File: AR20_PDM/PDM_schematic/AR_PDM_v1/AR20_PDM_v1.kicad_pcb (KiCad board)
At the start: 2 copper layers, 118 x 112 mm, 253 parts, among them IC1 TMUX1208PWR, J1 S_T_?, J2 1-776163-1, K1 DIPxx-1Cxx-51x, K2 DIPxx-1Cxx-51x, P1 B4B-PH-SM4-TB, Q1 BTS50025-1TAD, Q2 BTS50025-1TAD, Q3 BTS50025-1TAD, Q5 BTS50025-1TAD, Q6 BTS50025-1TAD, Q7 BTS50025-1TAD, Q8 BTS50025-1TAD, SW1 SW_DIP_x07, U1 ACM_2020, U10 N-MOS, U11 N-MOS, U12 P-MOS, U13 N-MOS, U14 N-MOS, U15 NMOS, U16 NMOS, U17 NMOS, U18 NMOS, U19 NMOS, U2 INA233, U20 NMOS, U21 NMOS, U22 NMOS, U23 NMOS, U24 NMOS, U25 NMOS, U26 NMOS, U27 NMOS, U28 NMOS, U29 INA233, U3 INA233, U30 INA233, U31 INA233, U32 Fet-P, U33 Fet-P, U34 Fet-P, U35 Fet-P, U36 Fet-P, U4 INA233, U5 INA233, U6 INA233, U7 INA233, U8 INA233, U9 TCA6424ARGJR

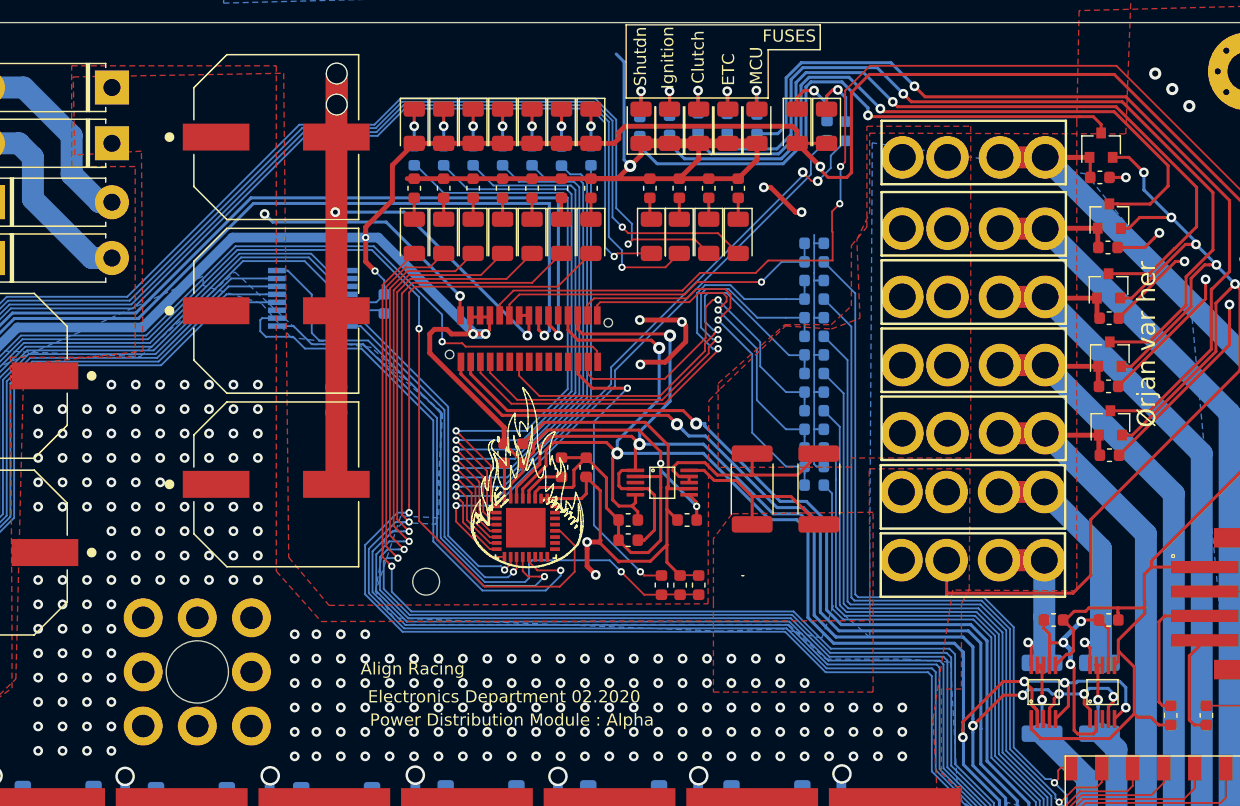
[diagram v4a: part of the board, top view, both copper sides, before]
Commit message: misc silkscreen changes
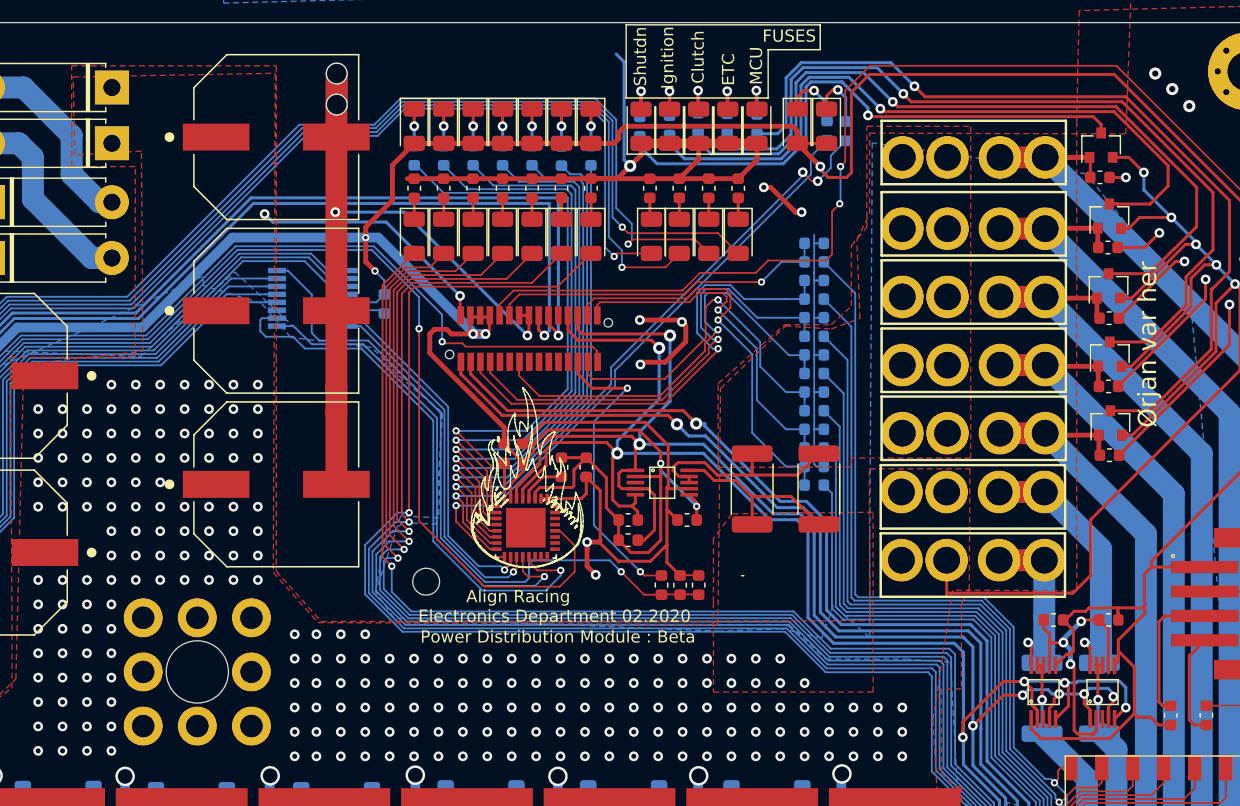
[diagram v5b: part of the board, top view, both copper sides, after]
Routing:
- net V+12V: vias 243 -> 244
- net (no net): vias 1 -> 0
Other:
- board text added: "Power Distribution Module : Beta"
- board text removed: "Power Distribution Module : Alpha"
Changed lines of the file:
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@@
     (thickness 1.6)
     (drawings 3807)
-    (tracks 3381)
+    (tracks 3380)
     (zones 0)
     (modules 253)
@@
     (34 B.Paste user hide)
     (35 F.Paste user hide)
-    (36 B.SilkS user hide)
-    (37 F.SilkS user hide)
+    (36 B.SilkS user)
+    (37 F.SilkS user)
     (38 B.Mask user hide)
     (39 F.Mask user hide)
@@
   (gr_line (start 88.955326 68.656325) (end 88.955666 69.225376) (layer F.SilkS) (width 0.06))
   (gr_arc (start 89.985704 70.027356) (end 87.409482 69.255581) (angle -5.477121106) (layer F.SilkS) (width 0.06))
-  (gr_text "Align Racing" (at 79.502 89.281) (layer F.SilkS)
+  (gr_text "Align Racing" (at 88.1507 83.3628) (layer F.SilkS)
     (effects (font (size 1 1) (thickness 0.15)))
   )
-  (gr_text "Power Distribution Module : Alpha" (at 87.63 93.472) (layer F.SilkS)
+  (gr_text "Power Distribution Module : Beta" (at 91.4019 86.6648) (layer F.SilkS)
     (effects (font (size 1 1) (thickness 0.15)))
   )
-  (gr_text "Ørjan var her" (at 139.6238 62.6999 90) (layer F.SilkS)
+  (gr_text "Ørjan var her" (at 139.7127 62.7126 90) (layer F.SilkS)
     (effects (font (size 1.5 1.5) (thickness 0.3)))
   )
-  (gr_text "Electronics Department 02.2020" (at 86.995 91.567) (layer F.SilkS)
+  (gr_text "Electronics Department 02.2020" (at 91.1225 84.963) (layer F.SilkS)
     (effects (font (size 1 1) (thickness 0.15)))
   )
@@
   (gr_line (start 151.8574 36.337) (end 33.857 36.337) (layer Edge.Cuts) (width 0.05))
   (gr_line (start 151.8574 148.336) (end 151.8574 36.337) (layer Edge.Cuts) (width 0.05))
-  (via (at 69.8373 96.4489) (size 0.8) (drill 0.4) (layers F.Cu B.Cu) (net 0))
+  (via (at 69.8373 96.4489) (size 0.8) (drill 0.4) (layers F.Cu B.Cu) (net 1))
   (via (at 69.8373 86.4489) (size 0.8) (drill 0.4) (layers F.Cu B.Cu) (net 1))
   (via (at 69.8373 88.4489) (size 0.8) (drill 0.4) (layers F.Cu B.Cu) (net 1))
@@
   (segment (start 114.554 48.133) (end 114.554 51.117502) (width 0.15) (layer B.Cu) (net 92))
   (segment (start 114.554 51.117502) (end 114.490502 51.181) (width 0.15) (layer B.Cu) (net 92))
-  (segment (start 113.8555 51.816002) (end 114.490502 51.181) (width 0.15) (layer F.Cu) (net 92))
-  (segment (start 113.9063 53.4924) (end 113.8555 53.4416) (width 0.15) (layer F.Cu) (net 92))
-  (segment (start 113.9063 55.8292) (end 113.9063 53.4924) (width 0.15) (layer F.Cu) (net 92))
-  (segment (start 108.6231 55.8292) (end 113.9063 55.8292) (width 0.15) (layer F.Cu) (net 92))
-  (segment (start 113.8555 53.4416) (end 113.8555 51.816002) (width 0.15) (layer F.Cu) (net 92))
+  (segment (start 113.3475 55.8292) (end 113.8555 55.3212) (width 0.15) (layer F.Cu) (net 92))
+  (segment (start 108.6231 55.8292) (end 113.3475 55.8292) (width 0.15) (layer F.Cu) (net 92))
   (segment (start 86.627 59.43) (end 87.764 58.293) (width 0.15) (layer F.Cu) (net 92))
-  (segment (start 87.764 58.293) (end 101.6 58.293) (width 0.15) (layer F.Cu) (net 92))
   (segment (start 86.627 60.33) (end 86.627 59.43) (width 0.15) (layer F.Cu) (net 92))
+  (segment (start 87.764 58.293) (end 101.6 58.293) (width 0.15) (layer F.Cu) (net 92))
+  (segment (start 113.8555 51.816002) (end 114.490502 51.181) (width 0.15) (layer F.Cu) (net 92))
   (segment (start 101.6 58.293) (end 103.047799 56.845201) (width 0.15) (layer F.Cu) (net 92))
+  (segment (start 113.8555 55.3212) (end 113.8555 51.816002) (width 0.15) (layer F.Cu) (net 92))
   (segment (start 103.047799 56.845201) (end 107.607099 56.845201) (width 0.15) (layer F.Cu) (net 92))
   (segment (start 107.607099 56.845201) (end 108.6231 55.8292) (width 0.15) (layer F.Cu) (net 92))
@@
         (xy 86.554081 127.579274) (xy 42.929581 125.293274) (xy 42.929581 114.688774) (xy 43.183581 107.576774) (xy 43.374081 93.606774)
         (xy 46.993581 90.114274) (xy 47.628581 64.714274) (xy 47.819081 64.333274) (xy 57.407581 63.253774) (xy 57.280581 46.870774)
-        (xy 51.819581 47.188274) (xy 51.692581 40.790649) (xy 68.932831 40.489024) (xy 69.345581 80.144774) (xy 72.647581 84.081774)
-        (xy 103.699081 83.954774) (xy 103.762581 67.317774) (xy 104.715081 66.333524) (xy 110.049081 61.190024) (xy 113.795581 61.444024)
+        (xy 51.819581 47.188274) (xy 51.692581 40.790649) (xy 68.2371 40.4876) (xy 68.0847 81.3816) (xy 71.7423 85.4964)
+        (xy 104.5083 85.6488) (xy 104.7115 67.4116) (xy 104.715081 66.333524) (xy 110.049081 61.190024) (xy 113.795581 61.444024)
         (xy 116.145081 60.570899) (xy 115.891081 54.125649) (xy 116.938831 51.950774) (xy 116.938425 45.39615) (xy 137.925175 45.45965)
         (xy 138.433581 31.884774) (xy 29.658081 33.154774) (xy 22.228581 152.788774) (xy 86.935081 150.439274)

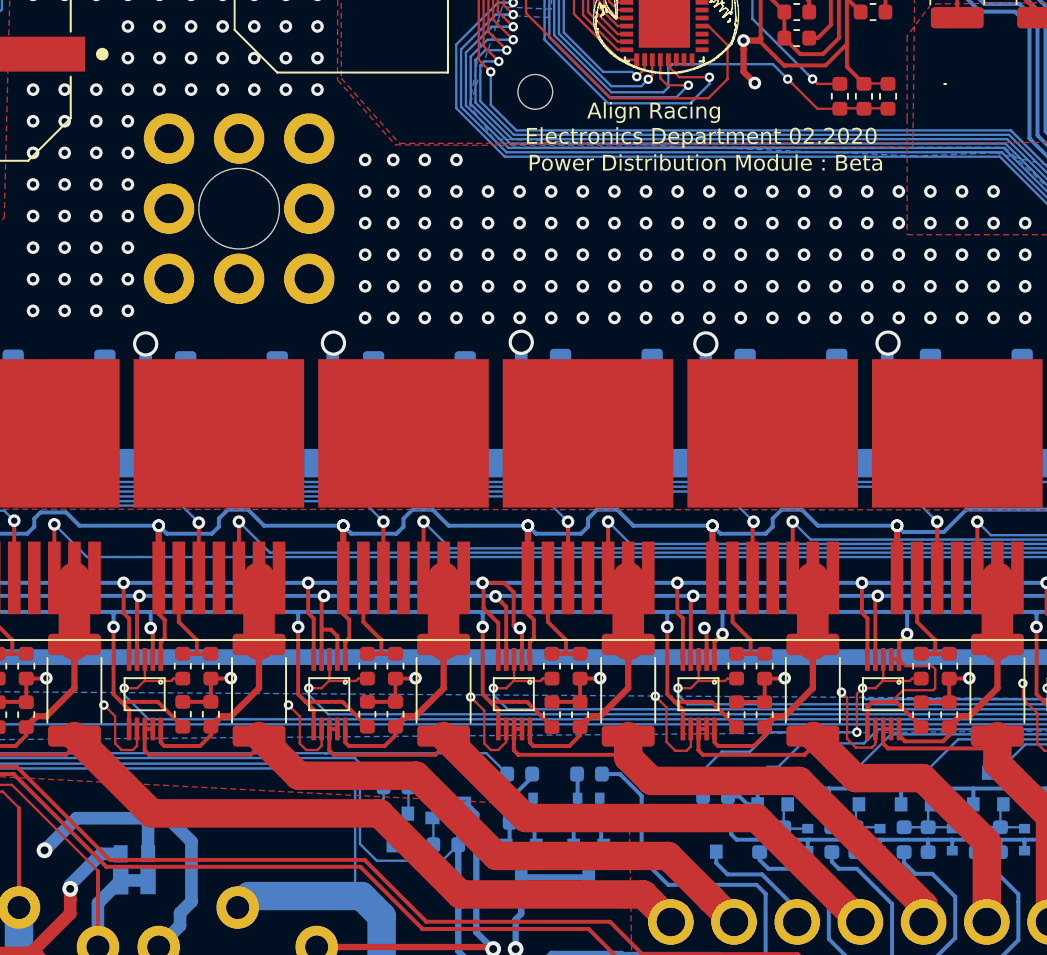
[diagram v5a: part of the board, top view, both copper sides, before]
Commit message: Gerber files generated, fixed diode footprint, added misc silkscreen
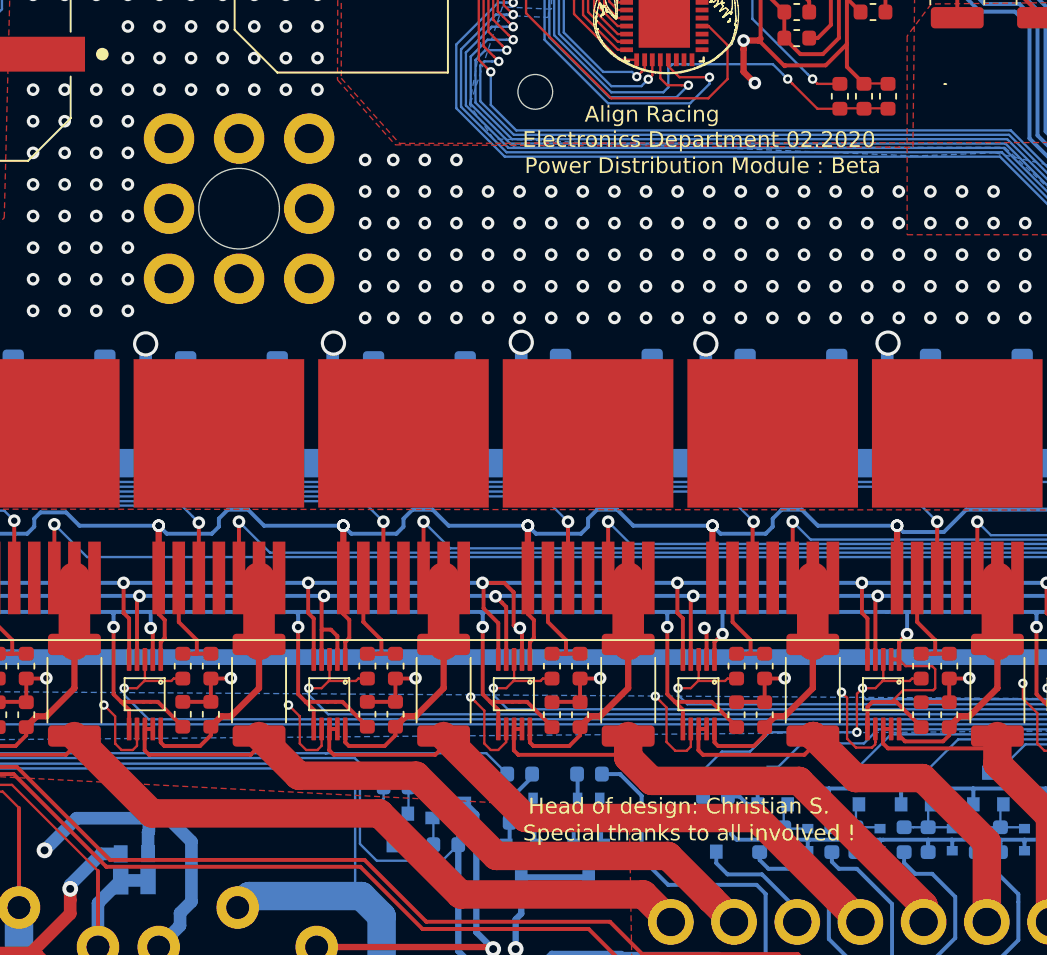
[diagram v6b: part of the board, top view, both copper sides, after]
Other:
- board text added: "Head of design: Christian S."
- board text added: "Special thanks to all involved !"
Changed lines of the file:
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@@
   (general
     (thickness 1.6)
-    (drawings 3807)
-    (tracks 3380)
+    (drawings 3809)
+    (tracks 3382)
     (zones 0)
     (modules 253)
@@
   )
   (setup
-    (last_trace_width 0.25)
+    (last_trace_width 0.8)
     (user_trace_width 0.15)
     (user_trace_width 0.25)
@@
     )
   )
+  (gr_text "Special thanks to all involved !" (at 90.3605 129.0574) (layer F.SilkS)
+    (effects (font (size 1 1) (thickness 0.15)))
+  )
+  (gr_text "Head of design: Christian S." (at 89.7001 127.3556) (layer F.SilkS)
+    (effects (font (size 1 1) (thickness 0.15)))
+  )
   (gr_text "Fuel\nACM" (at 80.2513 133.6675) (layer B.SilkS)
     (effects (font (size 1 1) (thickness 0.15)) (justify mirror))
@@
   (gr_line (start 88.955326 68.656325) (end 88.955666 69.225376) (layer F.SilkS) (width 0.06))
   (gr_arc (start 89.985704 70.027356) (end 87.409482 69.255581) (angle -5.477121106) (layer F.SilkS) (width 0.06))
-  (gr_text "Align Racing" (at 88.1507 83.3628) (layer F.SilkS)
+  (gr_text "Align Racing" (at 87.9983 83.566) (layer F.SilkS)
     (effects (font (size 1 1) (thickness 0.15)))
   )
-  (gr_text "Power Distribution Module : Beta" (at 91.4019 86.6648) (layer F.SilkS)
+  (gr_text "Power Distribution Module : Beta" (at 91.1987 86.8172) (layer F.SilkS)
     (effects (font (size 1 1) (thickness 0.15)))
   )
@@
     (effects (font (size 1.5 1.5) (thickness 0.3)))
   )
-  (gr_text "Electronics Department 02.2020" (at 91.1225 84.963) (layer F.SilkS)
+  (gr_text "Electronics Department 02.2020" (at 90.9701 85.1662) (layer F.SilkS)
     (effects (font (size 1 1) (thickness 0.15)))
   )
@@
   (segment (start 57.3659 128.1176) (end 56.1467 128.1176) (width 0.8) (layer B.Cu) (net 2))
   (segment (start 56.1467 128.1176) (end 51.5747 128.1176) (width 0.8) (layer B.Cu) (net 2))
-  (segment (start 56.0959 130.3538) (end 56.0959 128.1176) (width 0.8) (layer B.Cu) (net 2))
   (segment (start 124.5616 129.4765) (end 123.7615 129.4765) (width 0.25) (layer B.Cu) (net 2))
   (segment (start 125.2855 130.2004) (end 124.5616 129.4765) (width 0.25) (layer B.Cu) (net 2))
@@
   (segment (start 102.8827 105.6132) (end 102.91099 105.64149) (width 0.8) (layer B.Cu) (net 2))
   (segment (start 102.8827 102.7049) (end 102.8827 105.6132) (width 0.8) (layer B.Cu) (net 2))
+  (segment (start 56.1467 128.958) (end 56.1467 128.1176) (width 0.8) (layer B.Cu) (net 2))
+  (segment (start 56.0959 129.0088) (end 56.1467 128.958) (width 0.8) (layer B.Cu) (net 2))
+  (segment (start 56.0959 130.3538) (end 56.0959 129.0088) (width 0.8) (layer B.Cu) (net 2))
   (via (at 47.625 109.283506) (size 0.8) (drill 0.4) (layers F.Cu B.Cu) (net 3))
   (segment (start 47.625 112.909) (end 47.625 109.283506) (width 0.25) (layer F.Cu) (net 3))
@@
   (segment (start 51.1683 134.1628) (end 51.1683 133.295106) (width 0.8) (layer F.Cu) (net 17))
   (segment (start 48.6791 136.652) (end 51.1683 134.1628) (width 0.8) (layer F.Cu) (net 17))
-  (segment (start 53.124061 130.375546) (end 51.1683 132.331307) (width 0.8) (layer B.Cu) (net 17))
-  (segment (start 54.364061 130.375546) (end 53.124061 130.375546) (width 0.8) (layer B.Cu) (net 17))
-  (segment (start 51.1683 132.331307) (end 51.1683 132.588) (width 0.8) (layer B.Cu) (net 17))
   (segment (start 51.1683 133.295106) (end 51.1683 132.588) (width 0.8) (layer F.Cu) (net 17))
   (segment (start 110.963 144.907) (end 113.186 142.684) (width 0.4) (layer F.Cu) (net 17))
@@
   (segment (start 79.7339 131.8608) (end 79.7179 131.8768) (width 0.25) (layer B.Cu) (net 17))
   (segment (start 79.7179 131.8608) (end 83.9851 131.8608) (width 0.4) (layer B.Cu) (net 17))
+  (segment (start 51.1683 132.331307) (end 51.1683 132.588) (width 0.8) (layer B.Cu) (net 17))
+  (segment (start 53.124061 130.375546) (end 51.1683 132.331307) (width 0.8) (layer B.Cu) (net 17))
+  (segment (start 53.124061 130.375546) (end 54.364061 130.375546) (width 0.8) (layer B.Cu) (net 17))
   (via (at 82.042 44.831) (size 0.8) (drill 0.4) (layers F.Cu B.Cu) (net 18))
   (segment (start 82.042 43.431) (end 82.042 44.831) (width 0.25) (layer F.Cu) (net 18))
@@
   (segment (start 101.346 55.248) (end 100.206 56.388) (width 0.15) (layer F.Cu) (net 133))
   (via (at 39.0779 125.2728) (size 0.6) (drill 0.3) (layers F.Cu B.Cu) (net 133))
-  (segment (start 52.926434 133.493173) (end 54.364061 132.055546) (width 0.8) (layer B.Cu) (net 133))
   (segment (start 52.926434 136.271) (end 52.926434 133.493173) (width 0.8) (layer B.Cu) (net 133))
-  (segment (start 56.074154 132.055546) (end 56.0959 132.0338) (width 0.8) (layer B.Cu) (net 133))
-  (segment (start 54.364061 132.055546) (end 56.074154 132.055546) (width 0.8) (layer B.Cu) (net 133))
   (segment (start 52.926434 131.450534) (end 52.926434 136.271) (width 0.25) (layer F.Cu) (net 133))
   (segment (start 47.48211 126.00621) (end 52.926434 131.450534) (width 0.15) (layer F.Cu) (net 133))
@@
   (segment (start 77.9399 136.398) (end 76.8731 135.3312) (width 0.4) (layer B.Cu) (net 133))
   (segment (start 66.769434 136.271) (end 77.8129 136.271) (width 0.4) (layer F.Cu) (net 133))
+  (segment (start 56.074154 132.055546) (end 56.0959 132.0338) (width 0.8) (layer B.Cu) (net 133))
+  (segment (start 54.364061 132.055546) (end 56.074154 132.055546) (width 0.8) (layer B.Cu) (net 133))
+  (segment (start 52.926434 133.493173) (end 54.364061 132.055546) (width 0.8) (layer B.Cu) (net 133))
   (segment (start 116.1415 128.84) (end 116.1915 128.84) (width 0.15) (layer B.Cu) (net 134))
   (segment (start 113.6685 128.689) (end 114.6175 128.689) (width 0.15) (layer B.Cu) (net 134))
